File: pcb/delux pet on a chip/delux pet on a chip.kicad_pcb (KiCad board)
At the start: 4 copper layers, 76.2 x 63.5 mm, 69 parts, among them J1 USB_B, J2 Screw_Terminal_01x02, J3 Conn_02x15_Odd_Even, J4 Conn_02x15_Odd_Even, SW1 SW_Push, SW2 SW_Push, U1 93LCxxC, U2 FT2232HL, U3 LDL1117S33R, U4 TLV70012DDCR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

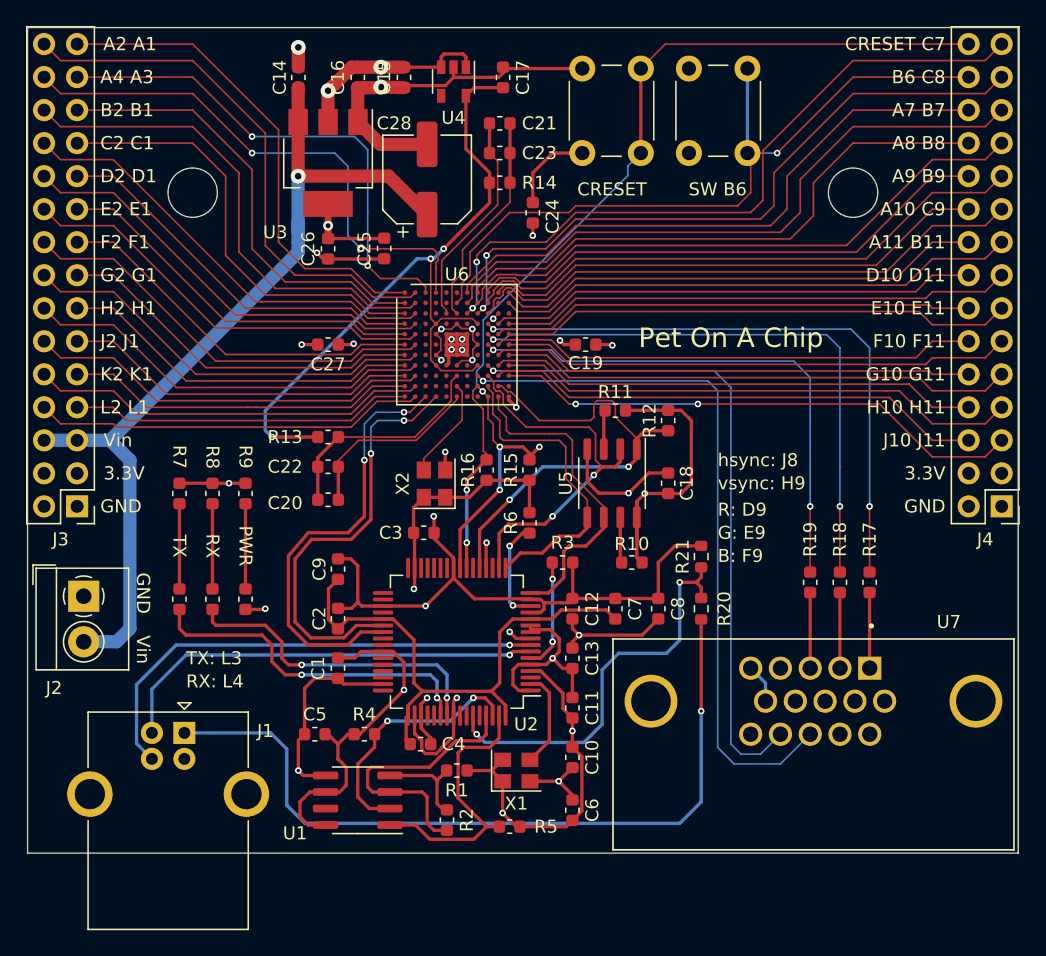
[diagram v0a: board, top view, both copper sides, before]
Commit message: Moved from KiCad 5 to KiCad 6, and fixed bad organization
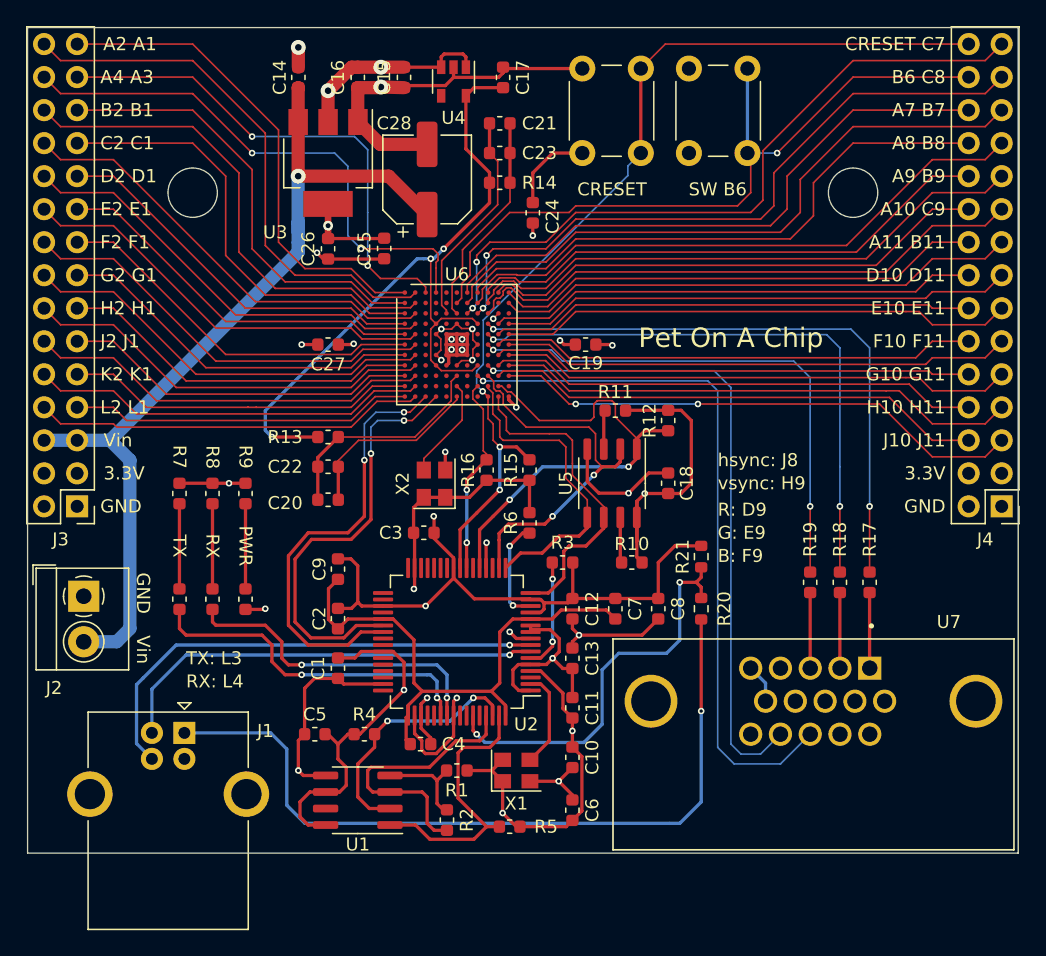
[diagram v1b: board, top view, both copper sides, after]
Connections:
- U1 pad 7: Net-(U1-Pad7) -> unconnected-(U1-Pad7)
- U2 pad 19: Net-(U2-Pad19) -> unconnected-(U2-Pad19)
- U2 pad 22: Net-(U2-Pad22) -> unconnected-(U2-Pad22)
- U2 pad 26: Net-(U2-Pad26) -> unconnected-(U2-Pad26)
- U2 pad 27: Net-(U2-Pad27) -> unconnected-(U2-Pad27)
- U2 pad 28: Net-(U2-Pad28) -> unconnected-(U2-Pad28)
- U2 pad 29: Net-(U2-Pad29) -> unconnected-(U2-Pad29)
- U2 pad 3: Net-(U2-Pad3) -> unconnected-(U2-Pad3)
- U2 pad 30: Net-(U2-Pad30) -> unconnected-(U2-Pad30)
- U2 pad 32: Net-(U2-Pad32) -> unconnected-(U2-Pad32)
- U2 pad 33: Net-(U2-Pad33) -> unconnected-(U2-Pad33)
- U2 pad 34: Net-(U2-Pad34) -> unconnected-(U2-Pad34)
- U2 pad 36: Net-(U2-Pad36) -> unconnected-(U2-Pad36)
- U2 pad 40: Net-(U2-Pad40) -> unconnected-(U2-Pad40)
- U2 pad 41: Net-(U2-Pad41) -> unconnected-(U2-Pad41)
- U2 pad 43: Net-(U2-Pad43) -> unconnected-(U2-Pad43)
- U2 pad 44: Net-(U2-Pad44) -> unconnected-(U2-Pad44)
- U2 pad 45: Net-(U2-Pad45) -> unconnected-(U2-Pad45)
- U2 pad 46: Net-(U2-Pad46) -> unconnected-(U2-Pad46)
- U2 pad 48: Net-(U2-Pad48) -> unconnected-(U2-Pad48)
- U2 pad 52: Net-(U2-Pad52) -> unconnected-(U2-Pad52)
- U2 pad 53: Net-(U2-Pad53) -> unconnected-(U2-Pad53)
- U2 pad 57: Net-(U2-Pad57) -> unconnected-(U2-Pad57)
- U2 pad 58: Net-(U2-Pad58) -> unconnected-(U2-Pad58)
- U2 pad 60: Net-(U2-Pad60) -> unconnected-(U2-Pad60)
- U6 pad A5: Net-(U6-PadA5) -> unconnected-(U6-PadA5)
- U6 pad A6: Net-(U6-PadA6) -> unconnected-(U6-PadA6)
- U6 pad B10: Net-(U6-PadB10) -> unconnected-(U6-PadB10)
- U6 pad B3: Net-(U6-PadB3) -> unconnected-(U6-PadB3)
- U6 pad B4: Net-(U6-PadB4) -> unconnected-(U6-PadB4)
- U6 pad B5: Net-(U6-PadB5) -> unconnected-(U6-PadB5)
- U6 pad C11: Net-(U6-PadC11) -> unconnected-(U6-PadC11)
- U6 pad C3: Net-(U6-PadC3) -> unconnected-(U6-PadC3)
- U6 pad C4: Net-(U6-PadC4) -> unconnected-(U6-PadC4)
- U6 pad D3: Net-(U6-PadD3) -> unconnected-(U6-PadD3)
- U6 pad D5: Net-(U6-PadD5) -> unconnected-(U6-PadD5)
- U6 pad D7: Net-(U6-PadD7) -> unconnected-(U6-PadD7)
- U6 pad E3: Net-(U6-PadE3) -> unconnected-(U6-PadE3)
- U6 pad E8: Net-(U6-PadE8) -> unconnected-(U6-PadE8)
- U6 pad F3: Net-(U6-PadF3) -> unconnected-(U6-PadF3)
- U6 pad F4: Net-(U6-PadF4) -> unconnected-(U6-PadF4)
- U6 pad G3: Net-(U6-PadG3) -> unconnected-(U6-PadG3)
- U6 pad G8: Net-(U6-PadG8) -> unconnected-(U6-PadG8)
- U6 pad G9: Net-(U6-PadG9) -> unconnected-(U6-PadG9)
- U6 pad H3: Net-(U6-PadH3) -> unconnected-(U6-PadH3)
- U6 pad H7: Net-(U6-PadH7) -> unconnected-(U6-PadH7)
- U6 pad J3: Net-(U6-PadJ3) -> unconnected-(U6-PadJ3)
- U6 pad J4: Net-(U6-PadJ4) -> unconnected-(U6-PadJ4)
- U6 pad J5: Net-(U6-PadJ5) -> unconnected-(U6-PadJ5)
- U6 pad J7: Net-(U6-PadJ7) -> unconnected-(U6-PadJ7)
- U6 pad K11: Net-(U6-PadK11) -> unconnected-(U6-PadK11)
- U6 pad K3: Net-(U6-PadK3) -> unconnected-(U6-PadK3)
- U6 pad K4: Net-(U6-PadK4) -> unconnected-(U6-PadK4)
- U6 pad K5: Net-(U6-PadK5) -> unconnected-(U6-PadK5)
- U6 pad K7: Net-(U6-PadK7) -> unconnected-(U6-PadK7)
- U6 pad L5: Net-(U6-PadL5) -> unconnected-(U6-PadL5)
- U6 pad L7: Net-(U6-PadL7) -> unconnected-(U6-PadL7)
- U6 pad L8: Net-(U6-PadL8) -> unconnected-(U6-PadL8)
- U7 pad 11: Net-(U7-Pad11) -> unconnected-(U7-Pad11)
- U7 pad 12: Net-(U7-Pad12) -> unconnected-(U7-Pad12)
- U7 pad 15: Net-(U7-Pad15) -> unconnected-(U7-Pad15)
- U7 pad 4: Net-(U7-Pad4) -> unconnected-(U7-Pad4)
- U7 pad 6: Net-(U7-Pad6) -> unconnected-(U7-Pad6)
- U7 pad 7: Net-(U7-Pad7) -> unconnected-(U7-Pad7)
- U7 pad 8: Net-(U7-Pad8) -> unconnected-(U7-Pad8)
- U7 pad 9: Net-(U7-Pad9) -> unconnected-(U7-Pad9)
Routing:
- net CRESET: track 75.9 -> 74.4 mm, vias 4 -> 3
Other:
- net class BAT removed
- net class Default removed
